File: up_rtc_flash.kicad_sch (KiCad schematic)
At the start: 14 parts, among them IC201 PCF8563T_5,518, IC202 W25Q128JVSIQTR, X201 PCIE-52P40H, X202 32.768 kHz, X203 TF-15×15, X204 CR1220-2ZX

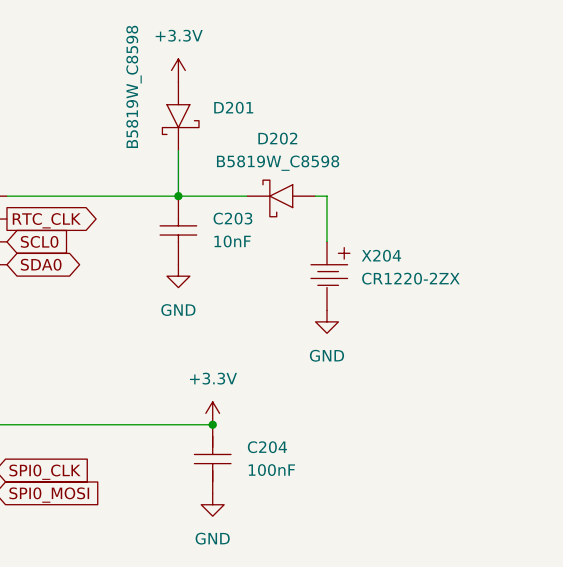
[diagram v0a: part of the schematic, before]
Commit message: Fix Power Label Mess.
Add Single Power_Output Symbol to each Power Network. All other Power-Labels are Power_Inputs.
ERC now shows no Power_Output/Input Errors.
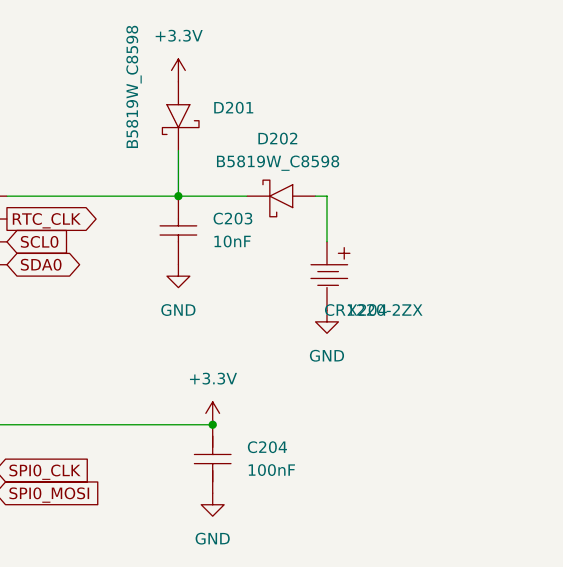
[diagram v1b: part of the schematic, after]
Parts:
- X204: footprint eduboardv2:BAT-SMD_CR1220-2ZX -> BAT-SMD_CR1220-2ZX
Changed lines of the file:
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@@
     (pin "2")
   )
-  (symbol (lib_name "+3.3V_4") (lib_id "eduboardv2:+3.3V") (at 154.94 177.8 0) (unit 1)
+  (symbol (lib_id "eduboardv2:+3.3V") (at 154.94 177.8 0) (unit 1)
     (in_bom yes) (on_board yes) (fields_autoplaced)
     (property "Reference" "#PWR0201" (id 0) (at 154.94 181.61 0)
@@
     (pin "1")
   )
-  (symbol (lib_name "GND_6") (lib_id "eduboardv2:GND") (at 220.98 133.35 270) (unit 1)
+  (symbol (lib_id "eduboardv2:GND") (at 220.98 133.35 270) (unit 1)
     (in_bom yes) (on_board yes)
     (property "Reference" "#PWR0208" (id 0) (at 214.63 133.35 0)
@@
   (symbol (lib_id "eduboardv2:CR1220-2ZX") (at 252.73 48.26 270) (unit 1)
     (in_bom yes) (on_board yes) (fields_autoplaced)
-    (property "Reference" "X204" (id 0) (at 256.54 46.0405 90)
+    (property "Reference" "X204" (id 0) (at 254.9495 52.07 90)
       (effects (font (size 1.27 1.27)) (justify left))
     )
-    (property "Value" "CR1220-2ZX" (id 1) (at 256.54 48.5805 90)
+    (property "Value" "CR1220-2ZX" (id 1) (at 252.4095 52.07 90)
       (effects (font (size 1.27 1.27)) (justify left))
     )
-    (property "Footprint" "eduboardv2:BAT-SMD_CR1220-2ZX" (id 2) (at 245.11 48.26 0)
-      (effects (font (size 1.27 1.27)) hide)
-    )
-    (property "Datasheet" "https://lcsc.com/product-detail/Battery-Holders-Clips-Contacts_Q-J-CR1220-2ZX_C969906.html" (id 3) (at 240.03 48.26 0)
-      (effects (font (size 1.27 1.27)) hide)
-    )
-    (property "Manufacturer" "Q&J" (id 4) (at 237.49 48.26 0)
-      (effects (font (size 1.27 1.27)) hide)
-    )
-    (property "LCSC Part" "C969906" (id 5) (at 234.95 48.26 0)
-      (effects (font (size 1.27 1.27)) hide)
-    )
-    (property "JLC Part" "Extended Part" (id 6) (at 232.41 48.26 0)
-      (effects (font (size 1.27 1.27)) hide)
-    )
-    (property "MPN" "CR1220-2ZX" (id 7) (at 247.65 48.26 0)
+    (property "Footprint" "BAT-SMD_CR1220-2ZX" (id 2) (at 266.7 50.8 0)
+      (effects (font (size 1.27 1.27)) hide)
+    )
+    (property "Datasheet" "https://lcsc.com/product-detail/Battery-Holders-Clips-Contacts_Q-J-CR1220-2ZX_C969906.html" (id 3) (at 243.84 39.37 0)
+      (effects (font (size 1.27 1.27)) hide)
+    )
+    (property "Manufacturer" "Q&J" (id 4) (at 256.54 34.29 0)
+      (effects (font (size 1.27 1.27)) hide)
+    )
+    (property "LCSC Part" "C969906" (id 5) (at 247.65 35.56 0)
+      (effects (font (size 1.27 1.27)) hide)
+    )
+    (property "JLC Part" "Extended Part" (id 6) (at 250.19 30.48 0)
+      (effects (font (size 1.27 1.27)) hide)
+    )
+    (property "MPN" "CR1220-2ZX" (id 7) (at 256.54 43.18 0)
       (effects (font (size 1.27 1.27)) hide)
     )
@@
     (pin "2")
   )
-  (symbol (lib_name "+3.3V_3") (lib_id "eduboardv2:+3.3V") (at 236.22 26.67 0) (unit 1)
+  (symbol (lib_id "eduboardv2:+3.3V") (at 236.22 26.67 0) (unit 1)
     (in_bom yes) (on_board yes) (fields_autoplaced)
     (property "Reference" "#PWR0209" (id 0) (at 236.22 30.48 0)
@@
     (pin "2")
   )
-  (symbol (lib_name "GND_7") (lib_id "eduboardv2:GND") (at 252.73 52.07 0) (unit 1)
+  (symbol (lib_id "eduboardv2:GND") (at 252.73 52.07 0) (unit 1)
     (in_bom yes) (on_board yes) (fields_autoplaced)
     (property "Reference" "#PWR0213" (id 0) (at 252.73 58.42 0)
@@
     (pin "1")
   )
-  (symbol (lib_name "+3.3V_2") (lib_id "eduboardv2:+3.3V") (at 162.56 177.8 0) (unit 1)
+  (symbol (lib_id "eduboardv2:+3.3V") (at 162.56 177.8 0) (unit 1)
     (in_bom yes) (on_board yes) (fields_autoplaced)
     (property "Reference" "#PWR0203" (id 0) (at 162.56 181.61 0)
@@
     (pin "1")
   )
-  (symbol (lib_name "GND_4") (lib_id "eduboardv2:GND") (at 236.22 46.99 0) (unit 1)
+  (symbol (lib_id "eduboardv2:GND") (at 236.22 46.99 0) (unit 1)
     (in_bom yes) (on_board yes) (fields_autoplaced)
     (property "Reference" "#PWR0210" (id 0) (at 236.22 53.34 0)

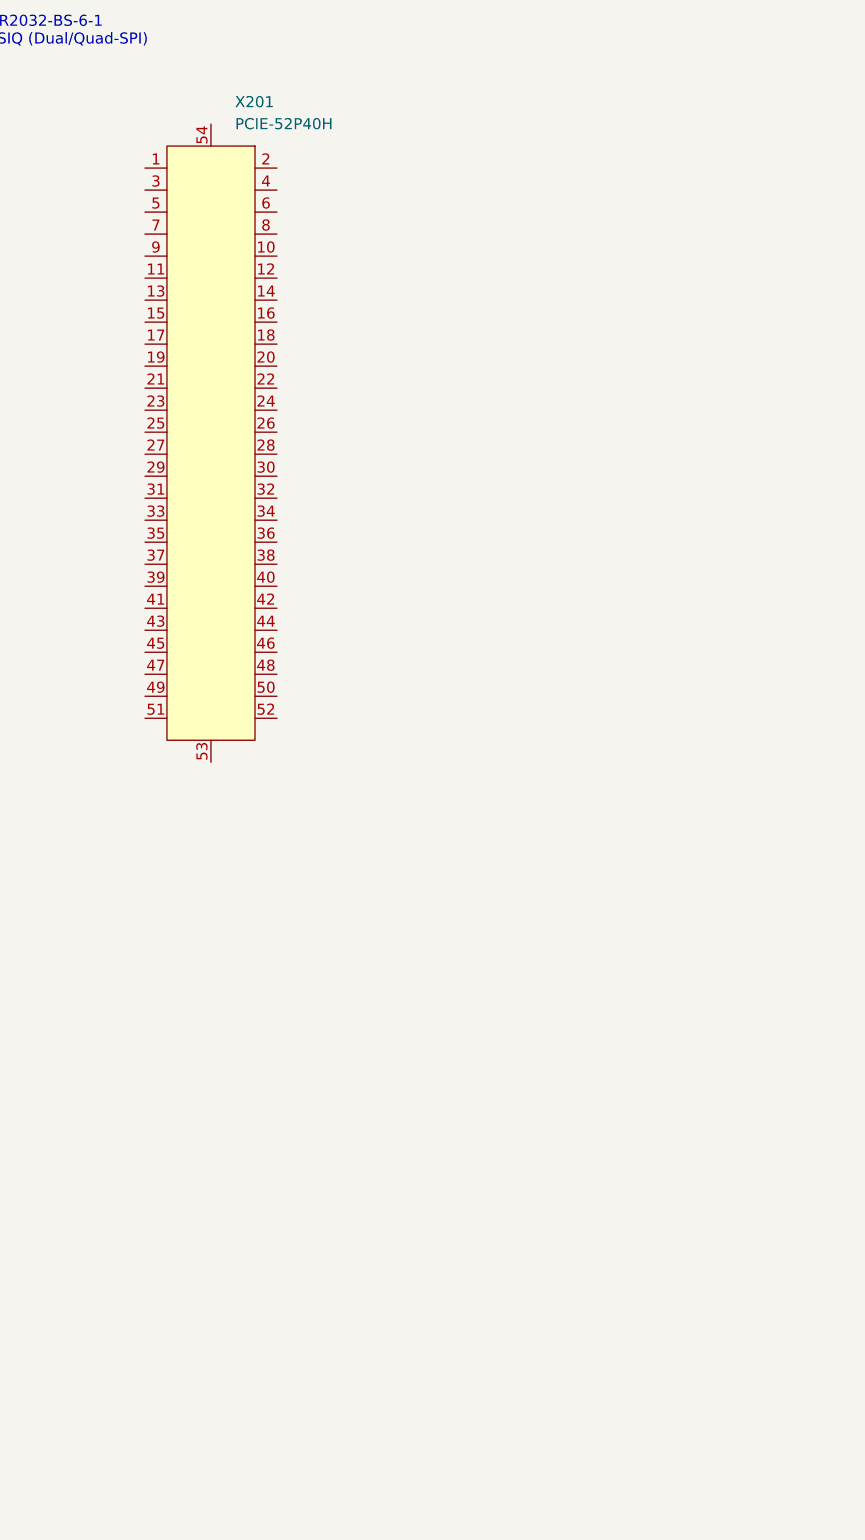
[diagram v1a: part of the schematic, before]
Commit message: Add Global Signals to UP page.
Audio Out missing,
USB Debug / USB Direct missing
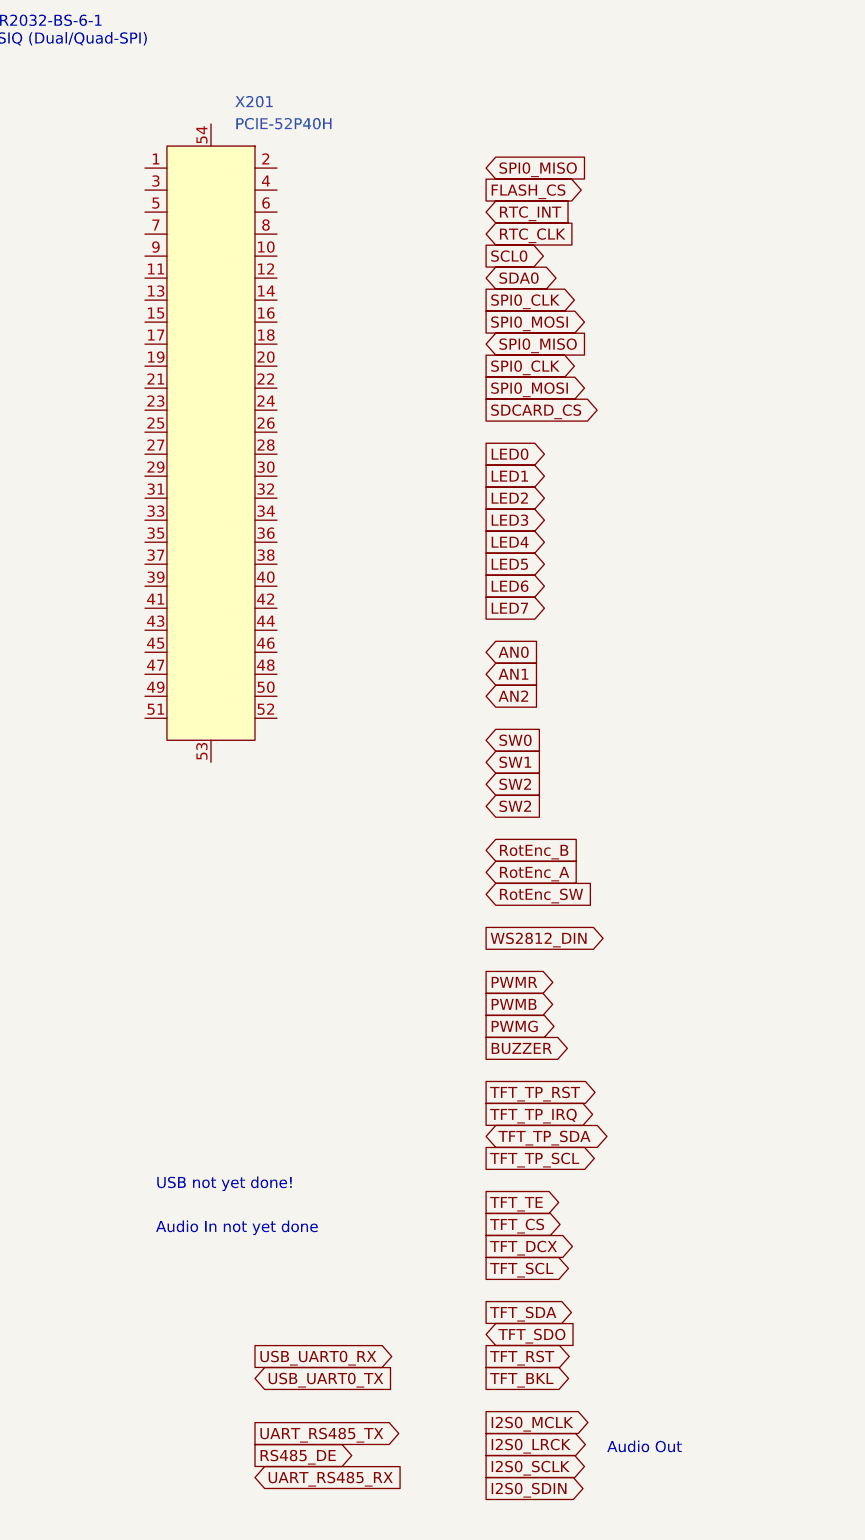
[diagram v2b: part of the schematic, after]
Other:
- note added: "Audio In not yet done"
- note added: "Audio Out"
- note added: "USB not yet done!"

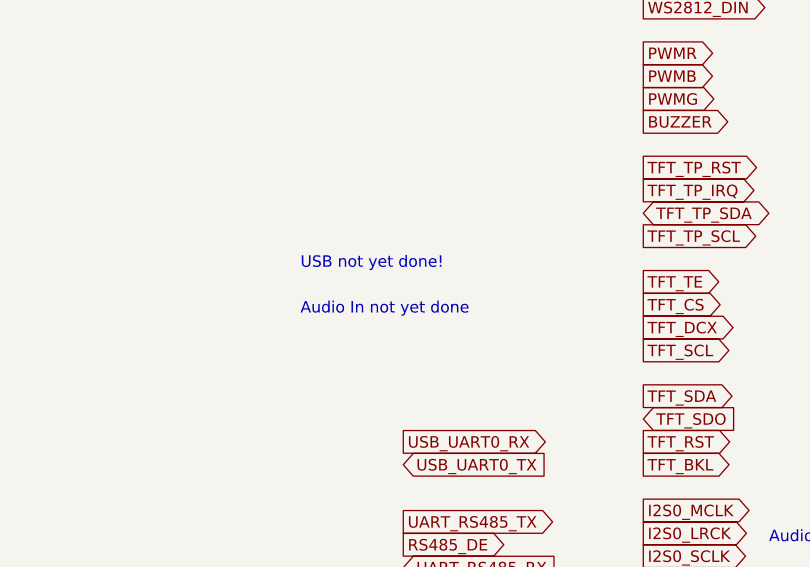
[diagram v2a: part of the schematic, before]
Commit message: Add new Page for USB Hub circuit.
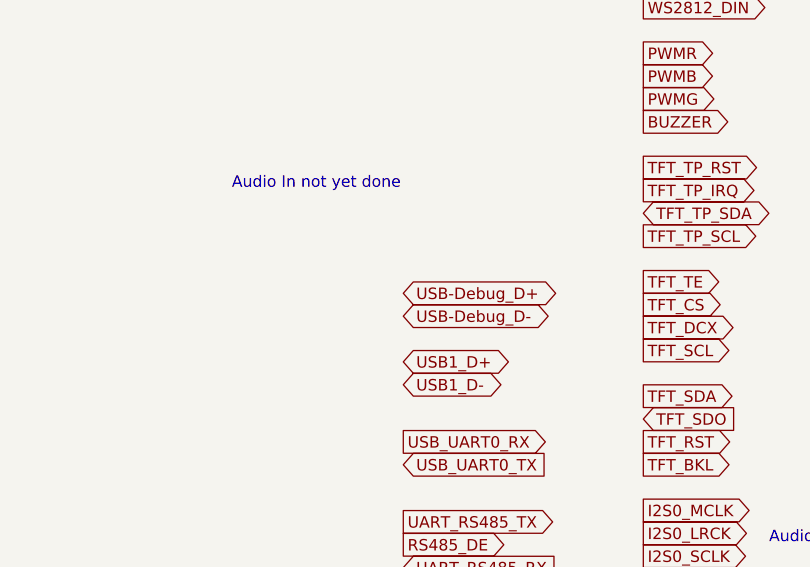
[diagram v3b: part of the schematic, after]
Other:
- note removed: "USB not yet done!"
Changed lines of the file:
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@@
     (effects (font (size 1.27 1.27)) (justify left bottom))
   )
-  (text "USB not yet done!\n" (at 49.53 156.21 0)
-    (effects (font (size 1.27 1.27)) (justify left bottom))
-  )
-  (text "Audio In not yet done\n" (at 49.53 161.29 0)
+  (text "Audio In not yet done\n" (at 41.91 147.32 0)
     (effects (font (size 1.27 1.27)) (justify left bottom))
   )
@@
     )
   )
+  (global_label "USB-Debug_D+" (shape bidirectional) (at 60.96 158.75 0) (fields_autoplaced)
+    (effects (font (size 1.27 1.27)) (justify left))
+    (property "Intersheet References" "${INTERSHEET_REFS}" (id 0) (at 78.3712 158.8294 0)
+      (effects (font (size 1.27 1.27)) (justify left) hide)
+    )
+  )
   (global_label "SDCARD_CS" (shape input) (at 220.98 113.03 180) (fields_autoplaced)
     (effects (font (size 1.27 1.27)) (justify right))
@@
     )
   )
+  (global_label "USB1_D-" (shape bidirectional) (at 60.96 168.91 0) (fields_autoplaced)
+    (effects (font (size 1.27 1.27)) (justify left))
+    (property "Intersheet References" "${INTERSHEET_REFS}" (id 0) (at 72.2026 168.8306 0)
+      (effects (font (size 1.27 1.27)) (justify left) hide)
+    )
+  )
   (global_label "SPI0_MISO" (shape input) (at 87.63 38.1 0) (fields_autoplaced)
     (effects (font (size 1.27 1.27)) (justify left))
@@
     )
   )
+  (global_label "USB1_D+" (shape bidirectional) (at 60.96 166.37 0) (fields_autoplaced)
+    (effects (font (size 1.27 1.27)) (justify left))
+    (property "Intersheet References" "${INTERSHEET_REFS}" (id 0) (at 72.2026 166.2906 0)
+      (effects (font (size 1.27 1.27)) (justify left) hide)
+    )
+  )
   (global_label "TFT_TP_SCL" (shape output) (at 87.63 152.4 0) (fields_autoplaced)
     (effects (font (size 1.27 1.27)) (justify left))
@@
       (effects (font (size 1.27 1.27)) (justify left) hide)
     )
+  )
+  (global_label "USB-Debug_D-" (shape bidirectional) (at 60.96 161.29 0) (fields_autoplaced)
+    (effects (font (size 1.27 1.27)) (justify left))
+    (property "Intersheet References" "${INTERSHEET_REFS}" (id 0) (at 78.3712 161.3694 0)
+      (effects (font (size 1.27 1.27)) (justify left) hide)
+    )
